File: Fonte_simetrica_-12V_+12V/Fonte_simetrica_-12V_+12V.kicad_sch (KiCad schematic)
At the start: 23 parts, among them Q4 AO3401A, U9 TPS65131RGER

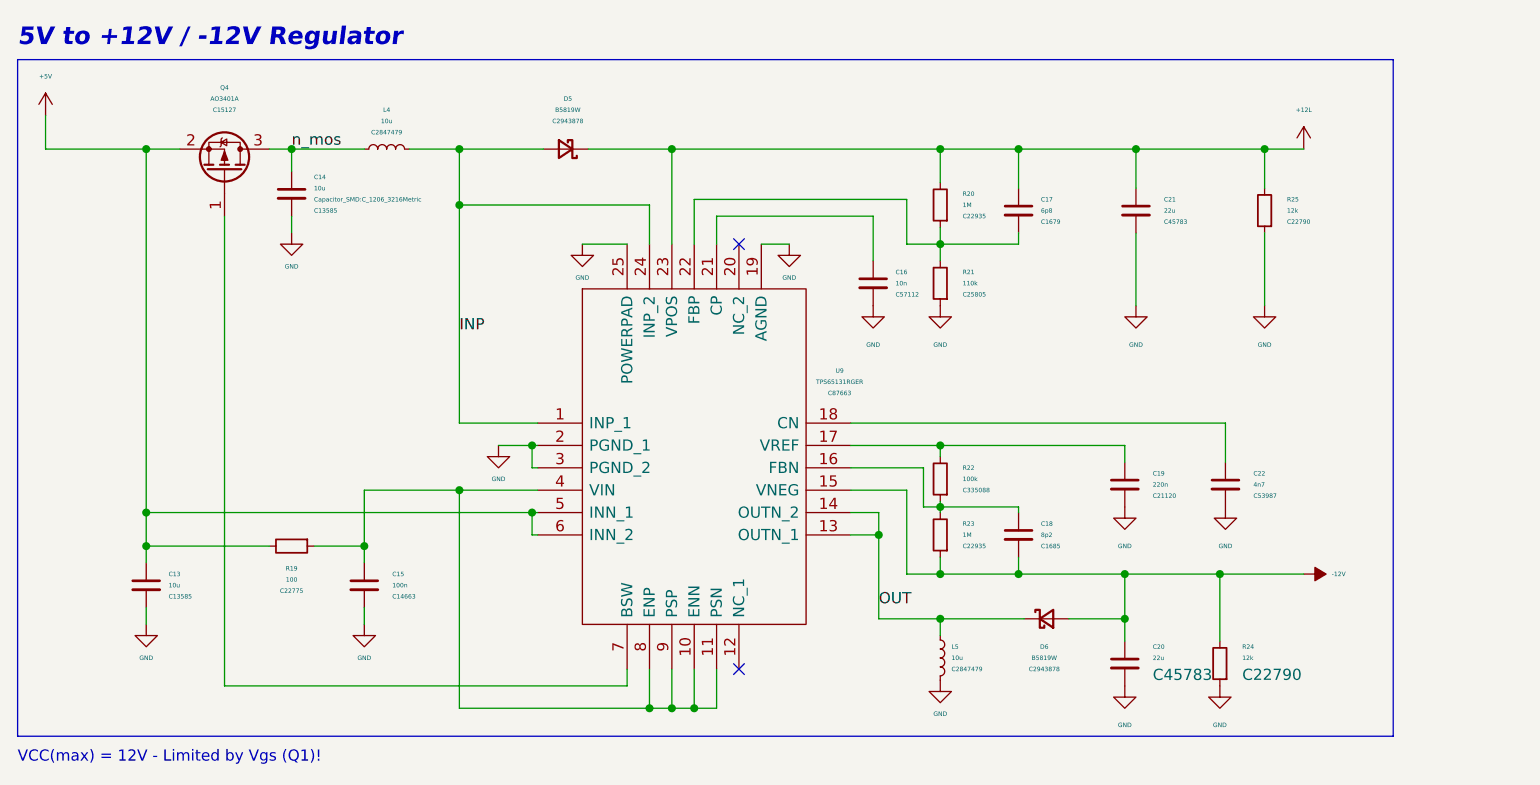
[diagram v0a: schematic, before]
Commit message: add power 12+ and 12-
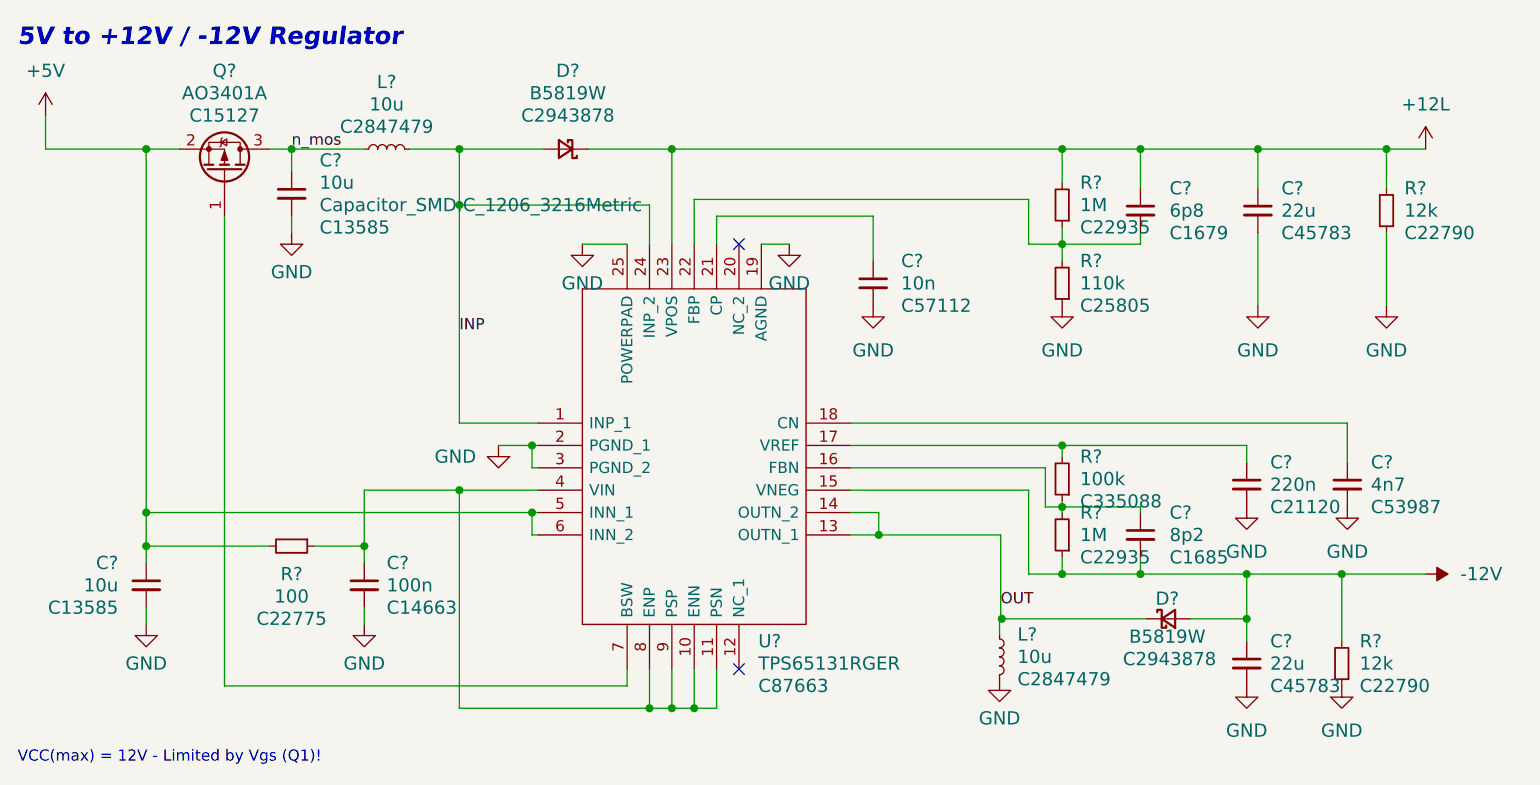
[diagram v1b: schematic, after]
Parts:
- renumbered C17 to C?, C14 to C?, C16 to C?, C13 to C?, C19 to C?, C21 to C?, C22 to C?, C15 to C?, C20 to C?, C18 to C?, D6 to D?, D5 to D?, L4 to L?, L5 to L?, Q4 to Q?, R24 to R?, R22 to R?, R21 to R?, R20 to R?, R23 to R?, R25 to R?, R19 to R?, U9 to U?
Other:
- moved on the sheet: C?, D?, L?, R?
